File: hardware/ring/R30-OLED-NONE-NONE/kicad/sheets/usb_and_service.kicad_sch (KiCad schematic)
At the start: 0 parts

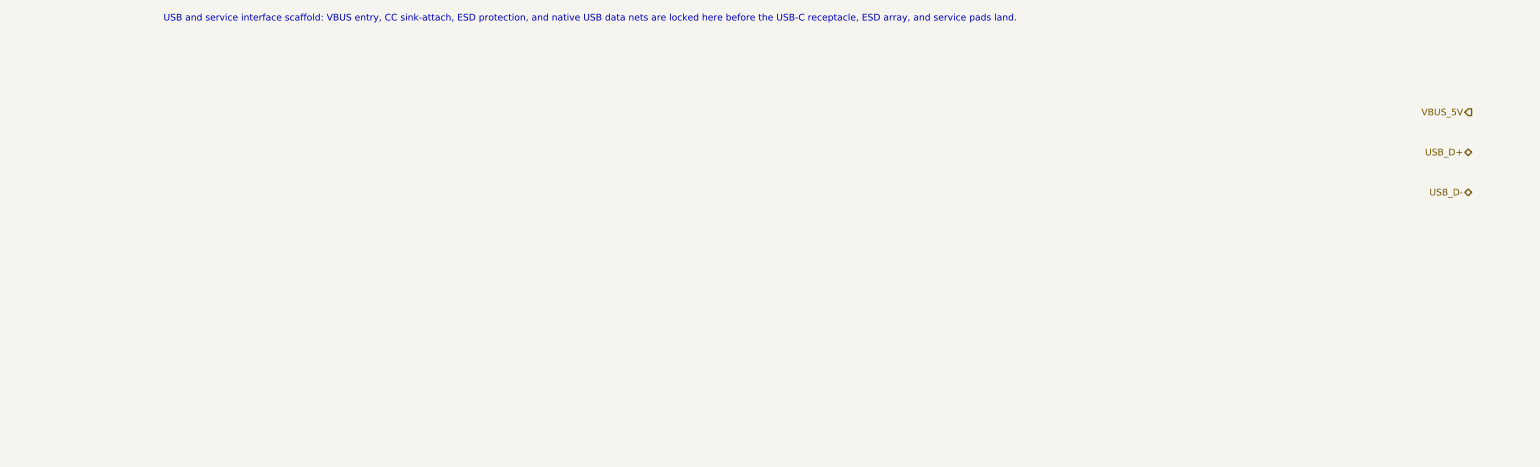
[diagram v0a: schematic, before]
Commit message: feat(hardware): populate R30 usb_and_service sub-sheet via kicad-sch-api
Adds J1 (USB-C 16-pin top-mount horizontal receptacle, GCT USB4105
class), R2 + R12 (5.1kΩ Rd CC1/CC2 pull-downs), and D1 (USBLC6-2SC6
dual-channel ESD array) with stock symbols + footprints. Wires:
  VBUS_5V — J1 A4/A9/B4/B9, D1.5
  USB_D+  — J1 A6/B6, D1.3, D1.4
  USB_D-  — J1 A7/B7, D1.1, D1.6
  CC1, CC2 — J1 A5/B5 → R2/R12 → GND
  GND     — J1 GND pins, D1.2, R2.2, R12.2, J1 SH (shield to GND)
  SBU1, SBU2 — no-connect markers (pin A8/B8)

Splits BOM R2 (Qty=2) row into R2 (CC1) + R12 (CC2) — same pattern as
the C1 → C1+C3 split (commit e1cb484), required because kicad-sch-api's
ref-format validator rejects "R2A"-style designators.

Extends project lib tables to include Connector + Power_Protection
(symbols) and Connector_USB (footprints).

ERC: /usb_and_service/ at 0 violations. Total ERC unchanged at 34
(pre-existing root-sheet label_dangling/endpoint_off_grid baseline).

Note: stock USB-C footprint is `USB4105`-class (top-mount horizontal,
16-pin, TH stakes). CAPTURE-BINDINGS.md cited `USB4215`; per the doc's
own commodity-source clause, USB4105 preserves the same retention class
and shell envelope and is acceptable.

Co-Authored-By: Claude Opus 4.7 (1M context) <noreply@anthropic.com>
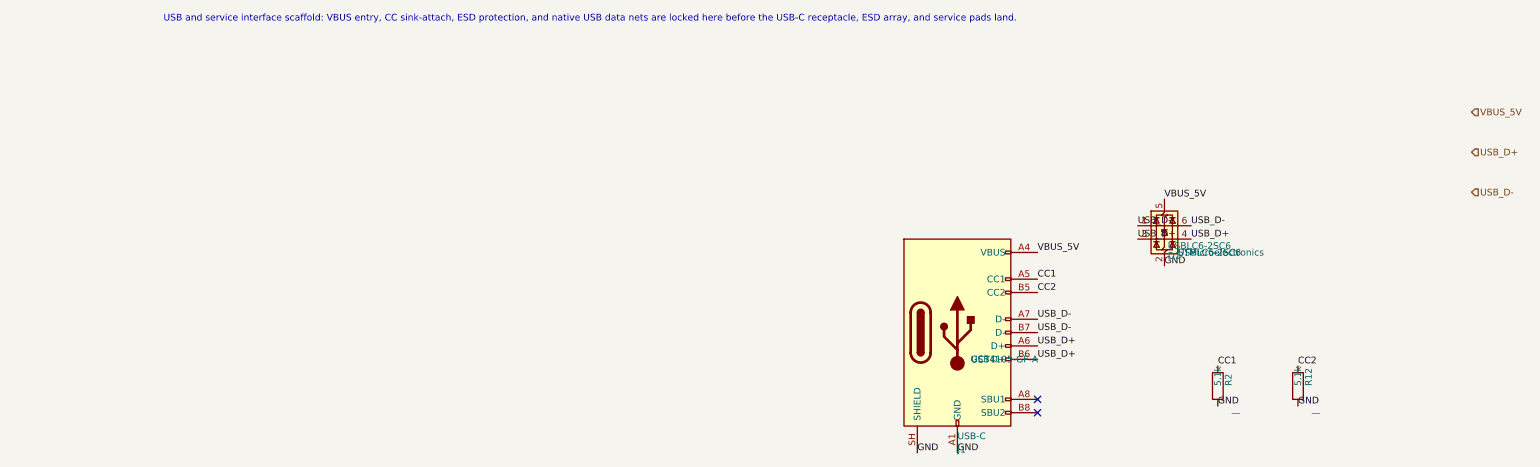
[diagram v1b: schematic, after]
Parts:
- added D1: USBLC6-2SC6, Package_TO_SOT_SMD:SOT-23-6, symbol Power_Protection:USBLC6-2SC6
- added J1: USB-C, Connector_USB:USB_C_Receptacle_GCT_USB4105-xx-A_16P_TopMnt_Horizontal, symbol Connector:USB_C_Receptacle_USB2.0_16P
- added R12, R2: 5.1k, Resistor_SMD:R_0402_1005Metric, symbol Device:R
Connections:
- net USB_D+: now also D1.3 (I/O2), D1.4 (I/O2), J1.A6 (D+), J1.B6 (D+)
- net USB_D-: now also D1.1 (I/O1), D1.6 (I/O1), J1.A7 (D-), J1.B7 (D-)
- net VBUS_5V: now also D1.5 (VBUS), J1.A4 (VBUS), J1.A9 (VBUS), J1.B4 (VBUS), J1.B9 (VBUS)
- new net CC1: J1.A5 (CC1), R2.1
- new net CC2: J1.B5 (CC2), R12.1
- new net GND: D1.2 (GND), J1.A1 (GND), J1.A12 (GND), J1.B1 (GND), J1.B12 (GND), J1.SH (SHIELD), R12.2, R2.2
- no-connect marks 0 -> 2
